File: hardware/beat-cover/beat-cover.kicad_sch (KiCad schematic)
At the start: 13 parts

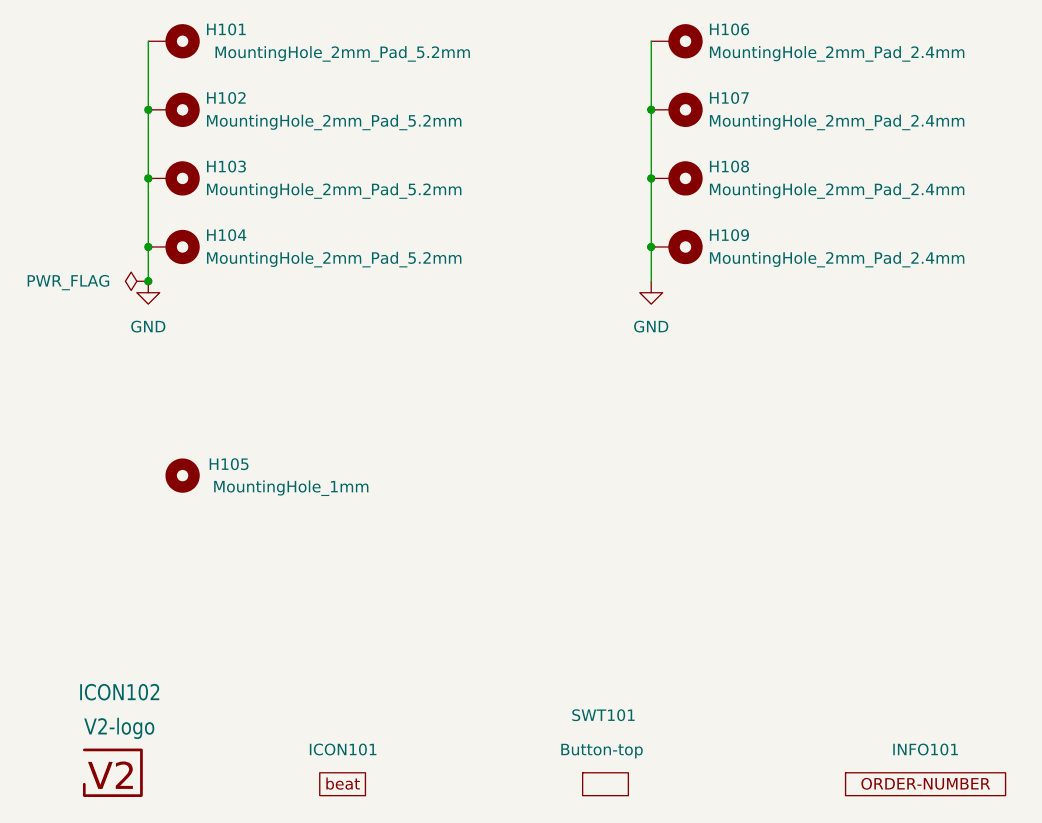
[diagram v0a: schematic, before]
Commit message: Replace Order_Number
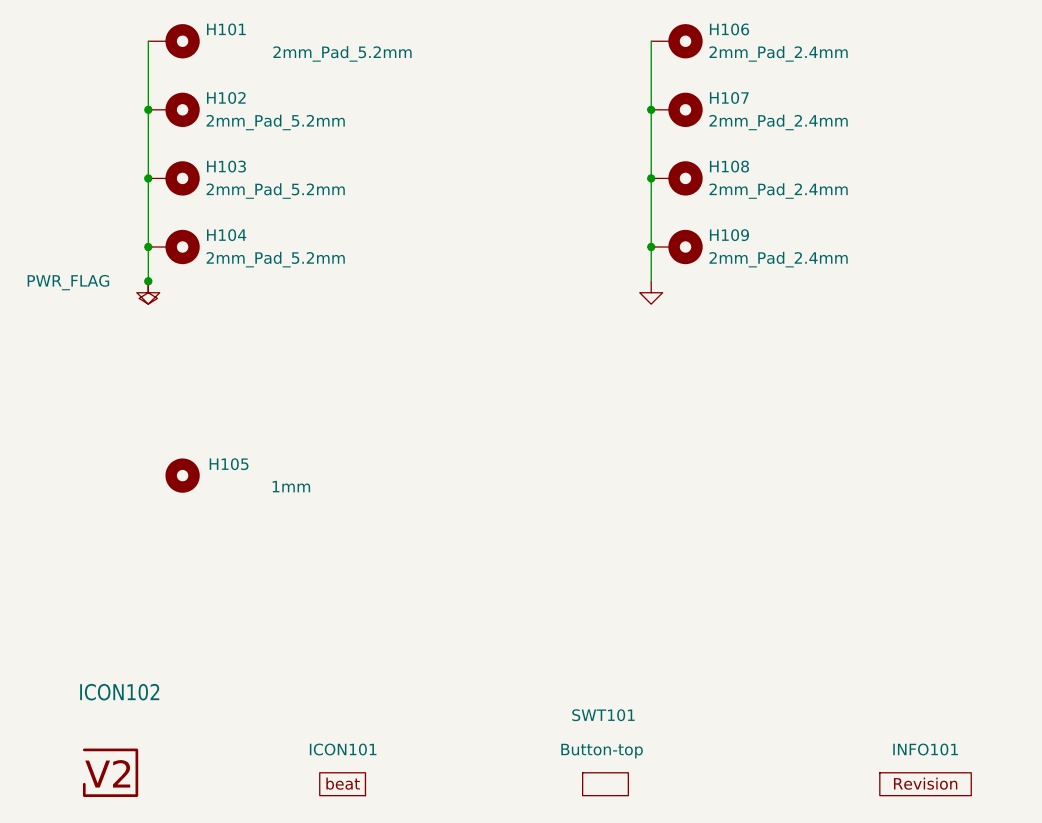
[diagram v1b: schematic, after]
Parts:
- H101, H102, H103, H104: value MountingHole_2mm_Pad_5.2mm -> 2mm_Pad_5.2mm
- H105: value MountingHole_1mm -> 1mm
- H106, H107, H108, H109: value MountingHole_2mm_Pad_2.4mm -> 2mm_Pad_2.4mm
- INFO101: value ORDER-NUMBER -> ~; footprint V2_Production:Order_Number -> V2_Production:Revision; symbol V2_Production:Order_Number -> V2_Production:Revision
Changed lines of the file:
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@@
 (kicad_sch
-	(version 20231120)
+	(version 20250114)
 	(generator "eeschema")
-	(generator_version "8.0")
+	(generator_version "9.0")
 	(paper "A4")
 	(title_block
 		(title "V2 beat")
-		(date "2023-09-12")
-		(rev "0")
+		(date "2026-02-13")
+		(rev "2023-09-12")
 		(company "Versio Duo")
 		(comment 1 "Cover")
@@
 	)
 	(symbol
-		(lib_id "power:GND")
+		(lib_id "V2_power:GND")
 		(at 105.41 85.09 0)
 		(unit 1)
@@
 					(size 1.27 1.27)
 				)
+				(hide yes)
 			)
 		)
@@
 		(at 107.95 66.04 270)
 		(unit 1)
-		(exclude_from_sim yes)
+		(exclude_from_sim no)
 		(in_bom no)
 		(on_board yes)
@@
 			)
 		)
-		(property "Value" "MountingHole_2mm_Pad_5.2mm"
+		(property "Value" "2mm_Pad_5.2mm"
 			(at 111.76 67.3099 90)
 			(effects
@@
 			)
 		)
-		(property "Description" ""
+		(property "Description" "Mounting Hole with connection"
 			(at 107.95 66.04 0)
 			(effects
@@
 		(at 163.83 58.42 270)
 		(unit 1)
-		(exclude_from_sim yes)
+		(exclude_from_sim no)
 		(in_bom no)
 		(on_board yes)
@@
 			)
 		)
-		(property "Value" "MountingHole_2mm_Pad_2.4mm"
+		(property "Value" "2mm_Pad_2.4mm"
 			(at 167.64 59.6899 90)
 			(effects
@@
 			)
 		)
-		(property "Datasheet" "~"
+		(property "Datasheet" ""
 			(at 163.83 58.42 0)
 			(effects
@@
 			)
 		)
-		(property "Description" ""
+		(property "Description" "Mounting Hole with connection"
 			(at 163.83 58.42 0)
 			(effects
@@
 	)
 	(symbol
-		(lib_id "power:GND")
+		(lib_id "V2_power:GND")
 		(at 161.29 85.09 0)
 		(unit 1)
@@
 					(size 1.27 1.27)
 				)
+				(hide yes)
 			)
 		)
@@
 	)
 	(symbol
-		(lib_id "V2_Production:Order_Number")
+		(lib_id "V2_Production:Revision")
 		(at 191.77 140.97 0)
 		(unit 1)
-		(exclude_from_sim yes)
+		(exclude_from_sim no)
 		(in_bom no)
 		(on_board yes)
@@
 			)
 		)
-		(property "Value" "ORDER-NUMBER"
+		(property "Value" "~"
 			(at 191.77 143.51 0)
 			(effects
@@
 			)
 		)
-		(property "Footprint" "V2_Production:Order_Number"
+		(property "Footprint" "V2_Production:Revision"
 			(at 191.77 146.05 0)
 			(effects
@@
 		(at 163.83 73.66 270)
 		(unit 1)
-		(exclude_from_sim yes)
+		(exclude_from_sim no)
 		(in_bom no)
 		(on_board yes)
@@
 			)
 		)
-		(property "Value" "MountingHole_2mm_Pad_2.4mm"
+		(property "Value" "2mm_Pad_2.4mm"
 			(at 167.64 74.9299 90)
 			(effects
@@
 			)
 		)
-		(property "Datasheet" "~"
+		(property "Datasheet" ""
 			(at 163.83 73.66 0)
 			(effects
@@
 			)
 		)
-		(property "Description" ""
+		(property "Description" "Mounting Hole with connection"
 			(at 163.83 73.66 0)
 			(effects
@@
 		(at 156.21 140.97 0)
 		(unit 1)
-		(exclude_from_sim yes)
+		(exclude_from_sim no)
 		(in_bom no)
 		(on_board yes)
@@
 			)
 		)
+		(property "Sim.Enable" "0"
+			(at 156.21 140.97 0)
+			(effects
+				(font
+					(size 1.27 1.27)
+				)
+				(hide yes)
+			)
+		)
 		(instances
 			(project "beat-cover"
@@
 		(at 107.95 81.28 270)
 		(unit 1)
-		(exclude_from_sim yes)
+		(exclude_from_sim no)
 		(in_bom no)
 		(on_board yes)
@@
 			)
 		)
-		(property "Value" "MountingHole_2mm_Pad_5.2mm"
+		(property "Value" "2mm_Pad_5.2mm"
 			(at 111.76 82.5499 90)
 			(effects
@@
 			)
 		)
-		(property "Description" ""
+		(property "Description" "Mounting Hole with connection"
 			(at 107.95 81.28 0)
 			(effects
@@
 		(at 163.83 81.28 270)
 		(unit 1)
-		(exclude_from_sim yes)
+		(exclude_from_sim no)
 		(in_bom no)
 		(on_board yes)
@@
 			)
 		)
-		(property "Value" "MountingHole_2mm_Pad_2.4mm"
+		(property "Value" "2mm_Pad_2.4mm"
 			(at 167.64 82.5499 90)
 			(effects
@@
 			)
 		)
-		(property "Datasheet" "~"
+		(property "Datasheet" ""
 			(at 163.83 81.28 0)
 			(effects
@@
 			)
 		)
-		(property "Description" ""
+		(property "Description" "Mounting Hole with connection"
 			(at 163.83 81.28 0)
 			(effects
@@
 		(at 107.95 58.42 270)
 		(unit 1)
-		(exclude_from_sim yes)
+		(exclude_from_sim no)
 		(in_bom no)
 		(on_board yes)
@@
 			)
 		)
-		(property "Value" "MountingHole_2mm_Pad_5.2mm"
+		(property "Value" "2mm_Pad_5.2mm"
 			(at 127 59.6899 90)
 			(effects
@@
 			)
 		)
-		(property "Description" ""
+		(property "Description" "Mounting Hole with connection"
 			(at 107.95 58.42 0)
 			(effects
@@
 		(at 127 140.97 0)
 		(unit 1)
-		(exclude_from_sim yes)
+		(exclude_from_sim no)
 		(in_bom no)
 		(on_board yes)
@@
 			)
 		)
+		(property "Sim.Enable" "0"
+			(at 127 140.97 0)
+			(effects
+				(font
+					(size 1.27 1.27)
+				)
+				(hide yes)
+			)
+		)
 		(instances
 			(project "beat-cover"
@@
 		(at 163.83 66.04 270)
 		(unit 1)
-		(exclude_from_sim yes)
+		(exclude_from_sim no)
 		(in_bom no)
 		(on_board yes)
@@
 			)
 		)
-		(property "Value" "MountingHole_2mm_Pad_2.4mm"
+		(property "Value" "2mm_Pad_2.4mm"
 			(at 167.64 67.3099 90)
 			(effects
@@
 			)
 		)
-		(property "Datasheet" "~"
+		(property "Datasheet" ""
 			(at 163.83 66.04 0)
 			(effects
@@
 			)
 		)
-		(property "Description" ""
+		(property "Description" "Mounting Hole with connection"
 			(at 163.83 66.04 0)
 			(effects
@@
 	)
 	(symbol
-		(lib_id "power:PWR_FLAG")
+		(lib_id "V2_power:PWR_FLAG")
 		(at 105.41 85.09 90)
 		(unit 1)
@@
 			)
 		)
-		(property "Datasheet" "~"
+		(property "Datasheet" ""
 			(at 105.41 85.09 0)
 			(effects
@@
 			)
 		)
-		(property "Description" ""
+		(property "Description" "Special symbol for telling ERC where power comes from"
 			(at 105.41 85.09 0)
 			(effects
@@
 		(at 109.22 106.68 0)
 		(unit 1)
-		(exclude_from_sim yes)
+		(exclude_from_sim no)
 		(in_bom no)
 		(on_board yes)
@@
 			)
 		)
-		(property "Value" "MountingHole_1mm"
+		(property "Value" "1mm"
 			(at 121.285 107.95 0)
 			(effects
@@
 			)
 		)
-		(property "Description" ""
+		(property "Description" "Mounting Hole without connection"
 			(at 109.22 106.68 0)
 			(effects
@@
 		(at 101.6 139.7 0)
 		(unit 1)
-		(exclude_from_sim yes)
+		(exclude_from_sim no)
 		(in_bom no)
 		(on_board yes)
@@
 					(size 1.778 1.5113)
 				)
+				(hide yes)
 			)
 		)
@@
 		(at 107.95 73.66 270)
 		(unit 1)
-		(exclude_from_sim yes)
+		(exclude_from_sim no)
 		(in_bom no)
 		(on_board yes)
@@
 			)
 		)
-		(property "Value" "MountingHole_2mm_Pad_5.2mm"
+		(property "Value" "2mm_Pad_5.2mm"
 			(at 111.76 74.9299 90)
 			(effects
@@
 			)
 		)
-		(property "Description" ""
+		(property "Description" "Mounting Hole with connection"
 			(at 107.95 73.66 0)
 			(effects
@@
 		)
 	)
+	(embedded_fonts no)
 )
